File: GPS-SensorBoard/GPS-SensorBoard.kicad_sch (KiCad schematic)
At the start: 19 parts, among them J1 ICSP, J2 POWER/CAN, J3 Conn_01x04, J4 Conn_01x04, U1 ATtiny841-SS, U2 MCP25625-x-SS, U3 74HC04

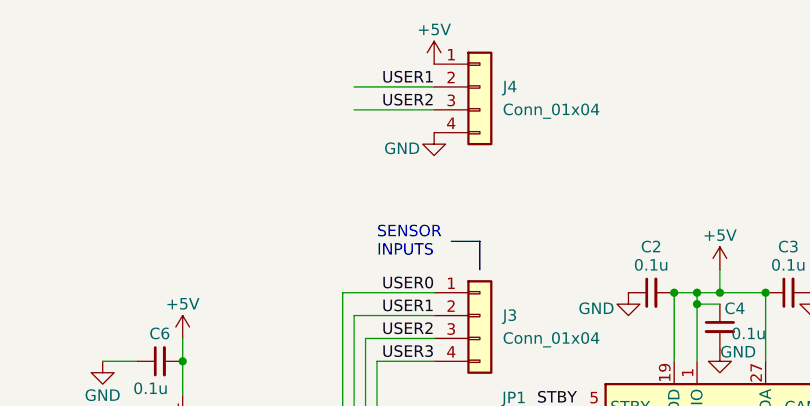
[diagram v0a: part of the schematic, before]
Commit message: Fixed grounds
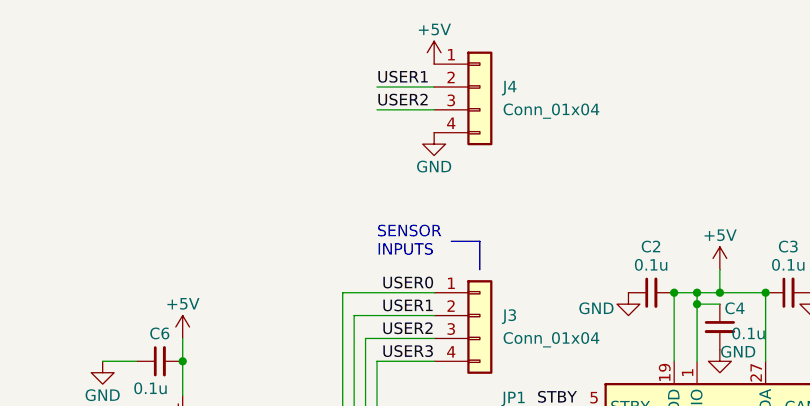
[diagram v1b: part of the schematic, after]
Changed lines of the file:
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@@
 	(wire
 		(pts
+			(xy 128.27 44.45) (xy 134.62 44.45)
+		)
+		(stroke
+			(width 0)
+			(type default)
+		)
+	)
+	(wire
+		(pts
 			(xy 95.25 147.32) (xy 100.33 147.32)
 		)
@@
 	(wire
 		(pts
-			(xy 125.73 44.45) (xy 134.62 44.45)
+			(xy 222.25 99.06) (xy 224.79 99.06)
 		)
 		(stroke
@@
 	(wire
 		(pts
-			(xy 222.25 99.06) (xy 224.79 99.06)
+			(xy 215.9 96.52) (xy 215.9 90.17)
 		)
 		(stroke
@@
 	(wire
 		(pts
-			(xy 215.9 96.52) (xy 215.9 90.17)
+			(xy 128.27 41.91) (xy 134.62 41.91)
 		)
 		(stroke
@@
 	(wire
 		(pts
-			(xy 125.73 41.91) (xy 134.62 41.91)
-		)
-		(stroke
-			(width 0)
-			(type default)
-		)
-	)
-	(wire
-		(pts
 			(xy 256.54 105.41) (xy 259.08 105.41)
 		)
@@
 	)
 	(label "USER2"
-		(at 134.62 44.45 180)
+		(at 128.27 44.45 0)
 		(fields_autoplaced yes)
 		(effects
@@
 				(size 1.27 1.27)
 			)
-			(justify right bottom)
+			(justify left bottom)
 		)
 	)
@@
 	)
 	(label "USER1"
-		(at 134.62 41.91 180)
+		(at 128.27 41.91 0)
 		(fields_autoplaced yes)
 		(effects
@@
 				(size 1.27 1.27)
 			)
-			(justify right bottom)
+			(justify left bottom)
 		)
 	)
@@
 		)
 		(property "Value" "GND"
-			(at 131.064 48.768 0)
+			(at 134.62 50.8 0)
 			(effects
 				(font

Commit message: Pushing stuff
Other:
- title: ATtiny Senor Board Template -> ATtiny Sensor Board Template
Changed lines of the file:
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@@
 	(paper "A4")
 	(title_block
-		(title "ATtiny Senor Board Template")
+		(title "ATtiny Sensor Board Template")
 		(date "2024-10-17")
 		(rev "1")

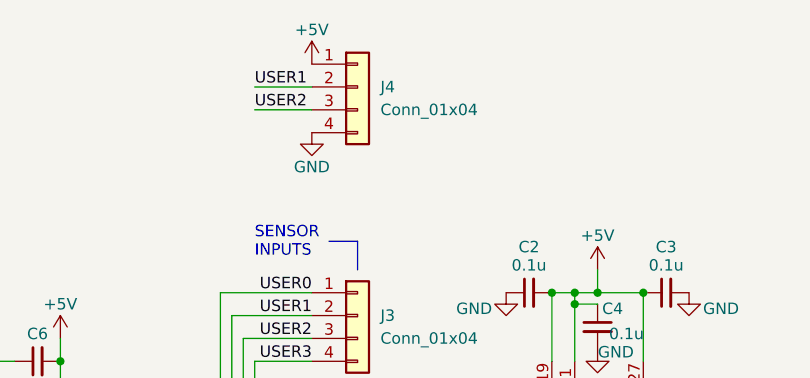
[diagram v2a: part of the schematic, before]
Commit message: GPS sensor board fix
Switched gnd and vcc
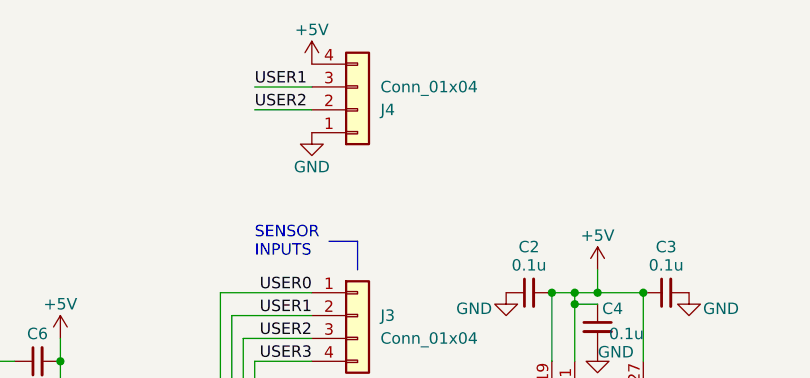
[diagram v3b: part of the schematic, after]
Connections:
- net +5V: now also J4.4 (Pin_4); no longer J4.1 (Pin_1)
- net GND: now also J4.1 (Pin_1); no longer J4.4 (Pin_4)
- net USER1: now also J4.3 (Pin_3); no longer J4.2 (Pin_2)
- net USER2: now also J4.2 (Pin_2); no longer J4.3 (Pin_3)
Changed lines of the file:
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@@
 	(symbol
 		(lib_id "Connector_Generic:Conn_01x04")
-		(at 139.7 41.91 0)
+		(at 139.7 44.45 0)
+		(mirror x)
 		(unit 1)
 		(exclude_from_sim no)
@@
 		(on_board yes)
 		(dnp no)
-		(fields_autoplaced yes)
 		(property "Reference" "J4"
-			(at 142.24 41.9099 0)
+			(at 142.24 44.4501 0)
 			(effects
 				(font
@@
 		)
 		(property "Value" "Conn_01x04"
-			(at 142.24 44.4499 0)
+			(at 142.24 41.9101 0)
 			(effects
 				(font
@@
 		)
 		(property "Footprint" "Connector_PinHeader_2.54mm:PinHeader_1x04_P2.54mm_Horizontal"
-			(at 139.7 41.91 0)
+			(at 139.7 44.45 0)
 			(effects
 				(font
@@
 		)
 		(property "Datasheet" "~"
-			(at 139.7 41.91 0)
+			(at 139.7 44.45 0)
 			(effects
 				(font
@@
 		)
 		(property "Description" "Generic connector, single row, 01x04, script generated (kicad-library-utils/schlib/autogen/connector/)"
-			(at 139.7 41.91 0)
+			(at 139.7 44.45 0)
 			(effects
 				(font
